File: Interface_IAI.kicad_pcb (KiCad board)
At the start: 2 copper layers, 54 x 63 mm, 20 parts, among them J1 ADWIN_DIO32, J2 ALIM_5V, J3 SCON_PULSE, J4 SCON_FEEDBACK, J5 ADWIN_CO4T, U1 AM26LS31CN, U2 AM26LS32ACN

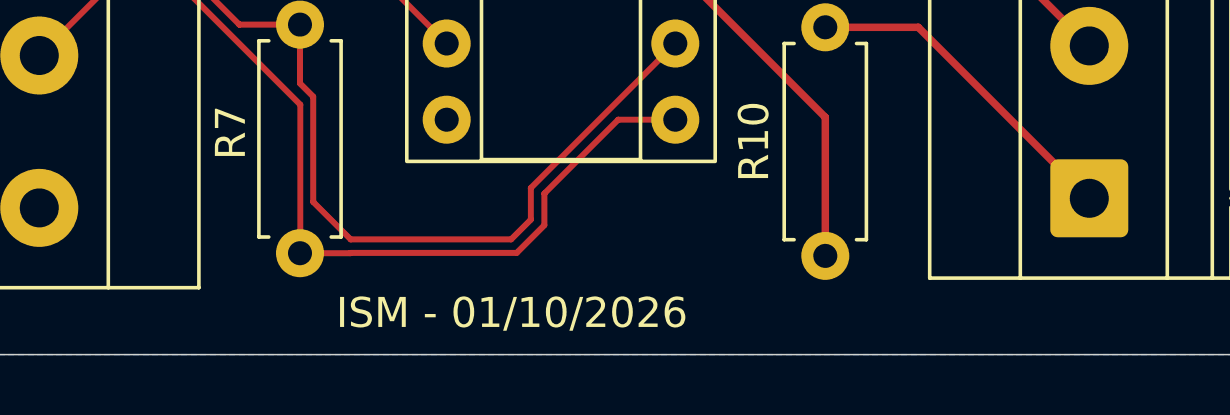
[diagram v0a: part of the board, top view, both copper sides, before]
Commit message: Update PCB silkscreen
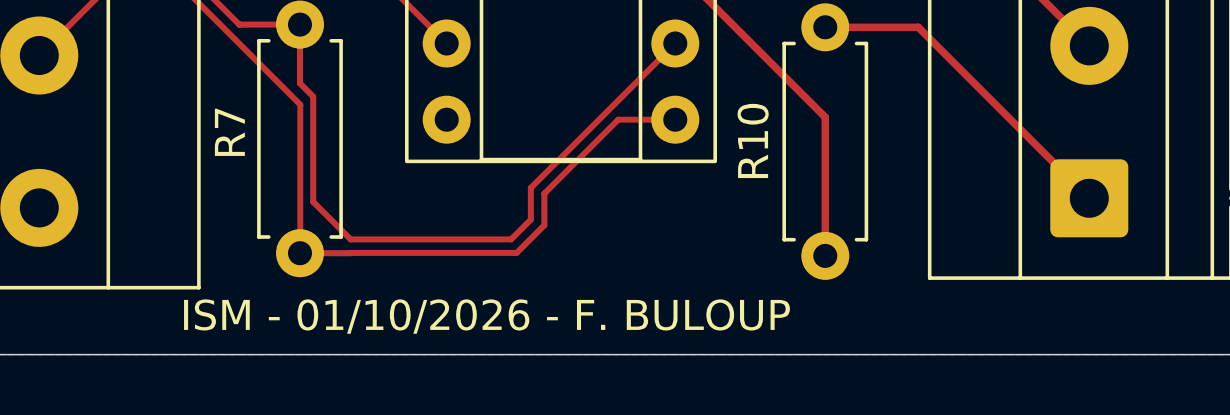
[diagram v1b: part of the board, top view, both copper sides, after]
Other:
- board text added: "ISM - 01/10/2026 - F. BULOUP"
- board text removed: "ISM - 01/10/2026"
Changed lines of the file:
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@@
 		(layer "Edge.Cuts")
 	)
-	(gr_text "ISM - 01/10/2026"
-		(at 69.6 112.2 0)
+	(gr_text "ISM - 01/10/2026 - F. BULOUP"
+		(at 64.4 112.3 0)
 		(layer "F.SilkS")
 		(effects

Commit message: Update board
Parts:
- removed C2: 10uF, Capacitor_THT:C_Disc_D5.0mm_W2.5mm_P5.00mm
- added C4: 10uF, Capacitor_THT:C_Disc_D5.0mm_W2.5mm_P5.00mm, F.Cu at (71.1, 82.6)
- added C5: 10uF 50V, Capacitor_THT:C_Disc_D5.0mm_W2.5mm_P5.00mm, F.Cu at (87.4, 87.3)
- added C6: 100nF, Capacitor_THT:C_Disc_D5.0mm_W2.5mm_P5.00mm, F.Cu at (82.6, 117.4)
- added D1: 1N5819, Diode_THT:D_DO-41_SOD81_P10.16mm_Horizontal, F.Cu at (94.3, 92.7)
- added H1: MountingHole, MountingHole:MountingHole_2.2mm_M2, F.Cu at (109.0, 53.0)
- added H2: MountingHole, MountingHole:MountingHole_2.2mm_M2, F.Cu at (109.0, 167.0)
- added H3: MountingHole, MountingHole:MountingHole_2.2mm_M2, F.Cu at (53.0, 53.0)
- added H4: MountingHole, MountingHole:MountingHole_2.2mm_M2, F.Cu at (53.1, 167.0)
- added J6: ADWin CO4-T, TerminalBlock_Phoenix:TerminalBlock_Phoenix_MKDS-1,5-4-5.08_1x04_P5.08mm_Horizontal, F.Cu at (100.6, 70.9)
- added R11: 10k, Resistor_THT:R_Axial_DIN0207_L6.3mm_D2.5mm_P7.62mm_Horizontal, F.Cu at (82.7, 137.9)
- added R12: 10k, Resistor_THT:R_Axial_DIN0207_L6.3mm_D2.5mm_P7.62mm_Horizontal, F.Cu at (83.0, 133.7)
- added R13: 10k, Resistor_THT:R_Axial_DIN0207_L6.3mm_D2.5mm_P7.62mm_Horizontal, F.Cu at (82.9, 128.9)
- added R14: 10k, Resistor_THT:R_Axial_DIN0207_L6.3mm_D2.5mm_P7.62mm_Horizontal, F.Cu at (82.9, 124.4)
- added R15: 10k, Resistor_THT:R_Axial_DIN0207_L6.3mm_D2.5mm_P7.62mm_Horizontal, F.Cu at (71.3, 145.6)
- added R16: 10k, Resistor_THT:R_Axial_DIN0207_L6.3mm_D2.5mm_P7.62mm_Horizontal, F.Cu at (71.5, 150.4)
- added R17: 10k, Resistor_THT:R_Axial_DIN0207_L6.3mm_D2.5mm_P7.62mm_Horizontal, F.Cu at (71.6, 155.4)
- added R18: 10k, Resistor_THT:R_Axial_DIN0207_L6.3mm_D2.5mm_P7.62mm_Horizontal, F.Cu at (71.5, 160.3)
- added R19: 2.2k, Resistor_THT:R_Axial_DIN0207_L6.3mm_D2.5mm_P7.62mm_Horizontal, F.Cu at (81.9, 145.6)
- added R20: 2.2k, Resistor_THT:R_Axial_DIN0207_L6.3mm_D2.5mm_P7.62mm_Horizontal, F.Cu at (82.2, 150.3)
- added R21: 2.2k, Resistor_THT:R_Axial_DIN0207_L6.3mm_D2.5mm_P7.62mm_Horizontal, F.Cu at (82.1, 155.4)
- added R22: 2.2k, Resistor_THT:R_Axial_DIN0207_L6.3mm_D2.5mm_P7.62mm_Horizontal, F.Cu at (82.1, 160.4)
- added U3: TBD62783APG, Package_DIP:DIP-18_W7.62mm_Socket, F.Cu at (79.5, 137.8)
- added U4: TSR1-2450E, Converter_DCDC:Converter_DCDC_TRACO_TSR-1_THT, F.Cu at (81.7, 83.1)
- J1: value ADWIN_DIO32 -> +24V; footprint TerminalBlock_Phoenix:TerminalBlock_Phoenix_MKDS-1,5-3-5.08_1x03_P5.08mm_Horizontal -> TerminalBlock_Phoenix:TerminalBlock_Phoenix_MKDS-1,5-2-5.08_1x02_P5.08mm_Horizontal
- J2: value ALIM_5V -> ADWIN_DIO32; footprint TerminalBlock_Phoenix:TerminalBlock_Phoenix_MKDS-1,5-2-5.08_1x02_P5.08mm_Horizontal -> TerminalBlock_Phoenix:TerminalBlock_Phoenix_MKDS-1,5-11-5.08_1x11_P5.08mm_Horizontal
- J3: value SCON_PULSE -> SCON_FEEDBACK; footprint TerminalBlock_Phoenix:TerminalBlock_Phoenix_MKDS-1,5-4-5.08_1x04_P5.08mm_Horizontal -> TerminalBlock_Phoenix:TerminalBlock_Phoenix_MKDS-1,5-7-5.08_1x07_P5.08mm_Horizontal
- J4: value SCON_FEEDBACK -> SCON_PULSE; footprint TerminalBlock_Phoenix:TerminalBlock_Phoenix_MKDS-1,5-7-5.08_1x07_P5.08mm_Horizontal -> TerminalBlock_Phoenix:TerminalBlock_Phoenix_MKDS-1,5-4-5.08_1x04_P5.08mm_Horizontal
- J5: value ADWIN_CO4T -> SCON_PIO; footprint TerminalBlock_Phoenix:TerminalBlock_Phoenix_MKDS-1,5-4-5.08_1x04_P5.08mm_Horizontal -> TerminalBlock_Phoenix:TerminalBlock_Phoenix_MKDS-1,5-10-5.08_1x10_P5.08mm_Horizontal
- U1: value AM26LS31CN -> AM26LS31
- U2: value AM26LS32ACN -> AM26LS32
- moved J2 84.8 mm to (100.8, 162.9)
- moved R4 52.9 mm to (82.0, 111.5), turned to 90 degrees
- moved R2 49.9 mm to (85.3, 103.9), turned to -90 degrees
- moved R10 41.1 mm to (84.9, 68.6), turned to 0 degrees
- moved R9 35.4 mm to (84.9, 63.7), turned to 0 degrees
- moved J5 34.6 mm to (61.4, 117.2), turned to -90 degrees
- moved U2 33.1 mm to (73.6, 54.3)
- moved C3 30.2 mm to (84.2, 54.1), turned to 0 degrees
- moved R1 29.3 mm to (89.1, 97.0)
- moved R7 29.1 mm to (81.0, 75.7), turned to 180 degrees
- moved R3 28.7 mm to (81.5, 100.6)
- moved R8 28.0 mm to (84.9, 60.3), turned to 0 degrees
- moved R6 27.1 mm to (69.7, 64.1)
- moved R5 26.9 mm to (69.7, 61.3)
- moved U1 22.0 mm to (70.0, 93.1), turned to 0 degrees
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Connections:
- J1 pad 1: /DIO_PULSE -> +24V
- J2 pad 1: +5V -> GND
- J2 pad 2: GND -> /DIO_ALM
- J3 pad 1: /SIGN_P -> /FB_A_N
- J3 pad 2: /SIGN_N -> /FB_A_P
- J3 pad 3: /PULSE_N -> /FB_B_P
- J3 pad 4: /PULSE_P -> /FB_B_N
- J4 pad 1: /FB_A_N -> /PULSE_P
- J4 pad 2: /FB_A_P -> /PULSE_N
- J4 pad 3: /FB_B_P -> /SIGN_N
- J4 pad 4: /FB_B_N -> /SIGN_P
- J5 pad 1: /CNT_Z -> +24V
- J5 pad 2: /CNT_B -> GND
- J5 pad 3: /CNT_A -> /SCON_CSTP
- J5 pad 4: GND -> /SCON_HOME
- U1 pad 4: +5V -> GND
- U2 pad 4: +5V -> GND
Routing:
- net +24V: track 0.00 -> 80.4 mm
- net /PULSE_P: track 44.9 -> 12.0 mm
- net /PULSE_N: track 39.5 -> 9.23 mm
- net /DIO_CSTP: track 0.00 -> 25.9 mm
- net /DIO_HOME: track 0.00 -> 23.8 mm
- net /DIO_RES: track 0.00 -> 23.7 mm
- net /DIO_SV: track 0.00 -> 23.1 mm
- net /DIO_INP: track 0.00 -> 22.8 mm
- net /DIO_ALM: track 0.00 -> 22.8 mm
- net /DIO_HEND: track 0.00 -> 22.7 mm
- net /DIO_SON: track 0.00 -> 22.7 mm
- net /SIGN_N: track 29.8 -> 9.23 mm
- net /DIO_PULSE: track 0.00 -> 20.0 mm
- net /PULSE_TTL: track 0.00 -> 16.7 mm
- net /VIN_REG: track 0.00 -> 16.5 mm
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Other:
- board size 54 x 63 mm -> 62 x 120 mm
- board text added: "+24V"
- board text added: "A"
- board text added: "ADWin - DIO32"
- board text added: "ADWin CO4-T"
- board text added: "ALIM+24V"
- board text added: "ALM"
- board text added: "B"
- board text added: "CSTP"
- board text added: "HEND"
- board text added: "HOME"
- board text added: "INP"
- board text added: "ISM - 04/10/2026 F.BULOUP"
- board text added: "PULSE_N"
- board text added: "PULSE_P"
- board text added: "RES"
- board text added: "SCON FEEDBACK"
- board text added: "SCON PIO"
- board text added: "SCON PULSE"
- board text added: "SIGN_N"
- board text added: "SIGN_P"
- board text added: "SON"
- board text added: "SV"
- board text added: "Z"
- board text removed: "+"
- board text removed: "+5V"
- board text removed: "ADWIN_CO4_T"
- board text removed: "ADWIN_DIO32"
- board text removed: "ALIM_5V"
- board text removed: "CNT_A"
- board text removed: "CNT_B"
- board text removed: "CNT_Z"
- board text removed: "ISM - 01/10/2026 - F. BULOUP"
- board text removed: "P_N"
- board text removed: "P_P"
- board text removed: "SCON_FEEDBACK"
- board text removed: "SCON_PULSE_SIGN"
- board text removed: "S_N"
- board text removed: "S_P"

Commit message: Modify BOM
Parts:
- C5: footprint Capacitor_THT:C_Disc_D5.0mm_W2.5mm_P5.00mm -> Capacitor_THT:C_Radial_D5.0mm_H11.0mm_P2.00mm
- moved C5 3.20 mm to (90.1, 85.5)
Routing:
- net /VIN_REG: track 16.5 -> 18.2 mm
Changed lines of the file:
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@@
 		(tags "THT Terminal Block Phoenix MKDS-1,5-11-5.08 pitch 5.08mm size 55.9x9.8mm drill 1.3mm pad 2.6mm")
 		(property "Reference" "J2"
-			(at 54.98 -0.18 0)
+			(at 54.843553 1.401374 0)
 			(layer "F.SilkS")
 			(effects
@@
 		)
 	)
-	(footprint "Capacitor_THT:C_Disc_D5.0mm_W2.5mm_P5.00mm"
+	(footprint "Capacitor_THT:C_Radial_D5.0mm_H11.0mm_P2.00mm"
 		(layer "F.Cu")
-		(at 87.398626 87.303553 90)
-		(descr "C, Disc series, Radial, pin pitch=5.00mm, diameter*width=5*2.5mm^2, Capacitor, http://cdn-reichelt.de/documents/datenblatt/B300/DS_KERKO_TC.pdf")
-		(tags "C Disc series Radial pin pitch 5.00mm diameter 5mm width 2.5mm Capacitor")
+		(at 90.07 85.54 90)
+		(descr "C, Radial series, Radial, pin pitch=2.00mm, diameter=5mm, height=11mm, Non-Polar Electrolytic Capacitor")
+		(tags "C Radial series Radial pin pitch 2.00mm diameter 5mm height 11mm Non-Polar Electrolytic Capacitor")
 		(property "Reference" "C5"
-			(at 6.9 -0.2 0)
+			(at 1 -3.75 90)
 			(layer "F.SilkS")
 			(effects
@@
 		)
 		(property "Value" "10uF 50V"
-			(at 2.5 2.5 90)
+			(at 1 3.75 90)
 			(layer "F.Fab")
 			(effects
@@
 		(attr through_hole)
 		(duplicate_pad_numbers_are_jumpers no)
-		(fp_line
-			(start 5.12 -1.37)
-			(end 5.12 -1.033)
-			(stroke
-				(width 0.12)
-				(type solid)
-			)
-			(layer "F.SilkS")
-		)
-		(fp_line
-			(start -0.12 -1.37)
-			(end 5.12 -1.37)
-			(stroke
-				(width 0.12)
-				(type solid)
-			)
-			(layer "F.SilkS")
-		)
-		(fp_line
-			(start -0.12 -1.033)
-			(end -0.12 -1.37)
-			(stroke
-				(width 0.12)
-				(type solid)
-			)
-			(layer "F.SilkS")
-		)
-		(fp_line
-			(start 5.12 1.033)
-			(end 5.12 1.37)
-			(stroke
-				(width 0.12)
-				(type solid)
-			)
-			(layer "F.SilkS")
-		)
-		(fp_line
-			(start 5.12 1.37)
-			(end -0.12 1.37)
-			(stroke
-				(width 0.12)
-				(type solid)
-			)
-			(layer "F.SilkS")
-		)
-		(fp_line
-			(start -0.12 1.37)
-			(end -0.12 1.033)
+		(fp_circle
+			(center 1 0)
+			(end 3.62 0)
 			(stroke
 				(width 0.12)
 				(type solid)
 			)
+			(fill no)
 			(layer "F.SilkS")
 		)
-		(fp_rect
-			(start -1.05 -1.5)
-			(end 6.05 1.5)
+		(fp_circle
+			(center 1 0)
+			(end 3.75 0)
 			(stroke
 				(width 0.05)
@@
 			(layer "F.CrtYd")
 		)
-		(fp_rect
-			(start 0 -1.25)
-			(end 5 1.25)
+		(fp_circle
+			(center 1 0)
+			(end 3.5 0)
 			(stroke
 				(width 0.1)
@@
 		)
 		(fp_text user "${REFERENCE}"
-			(at 2.5 0 90)
+			(at 1 0 90)
 			(layer "F.Fab")
 			(effects
@@
 		)
 		(pad "2" thru_hole circle
-			(at 5 0 90)
+			(at 2 0 90)
 			(size 1.6 1.6)
 			(drill 0.8)
@@
 		)
 		(embedded_fonts no)
-		(model "${KICAD10_3DMODEL_DIR}/Capacitor_THT.3dshapes/C_Disc_D5.0mm_W2.5mm_P5.00mm.step"
+		(model "${KICAD10_3DMODEL_DIR}/Capacitor_THT.3dshapes/C_Radial_D5.0mm_H11.0mm_P2.00mm.step"
 			(offset
 				(xyz 0 0 0)
@@
 	)
 	(segment
-		(start 87.398626 87.303553)
-		(end 88.859109 87.303553)
+		(start 90.07 85.54)
+		(end 84.150073 85.54)
 		(width 1)
 		(layer "F.Cu")
@@
 	)
 	(segment
-		(start 87.398626 87.303553)
-		(end 85.913626 87.303553)
+		(start 94.26 92.704444)
+		(end 94.26 89.73)
 		(width 1)
 		(layer "F.Cu")
@@
 	)
 	(segment
-		(start 85.913626 87.303553)
+		(start 84.150073 85.54)
 		(end 81.731126 83.121053)
 		(width 1)
@@
 	)
 	(segment
-		(start 88.859109 87.303553)
-		(end 94.26 92.704444)
+		(start 94.26 89.73)
+		(end 90.07 85.54)
 		(width 1)
 		(layer "F.Cu")

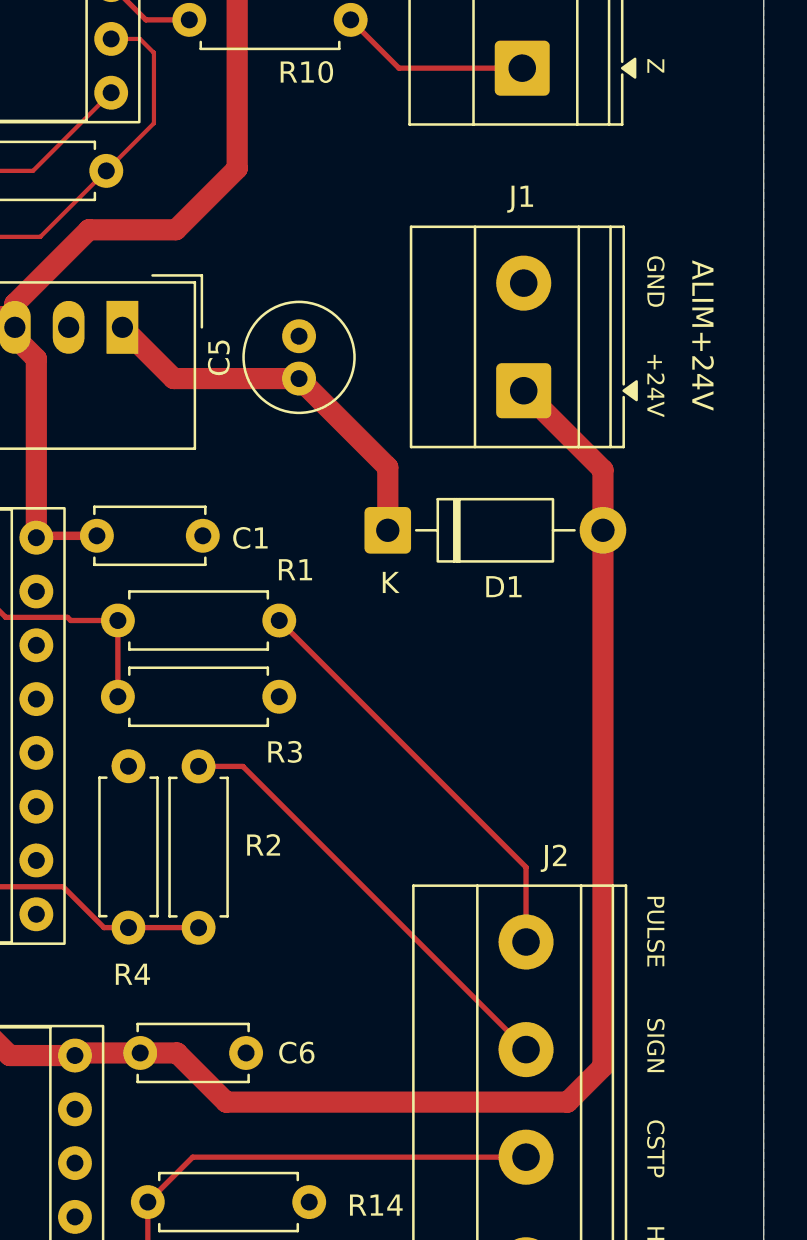
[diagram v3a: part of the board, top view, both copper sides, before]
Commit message: Add DEL Alim.
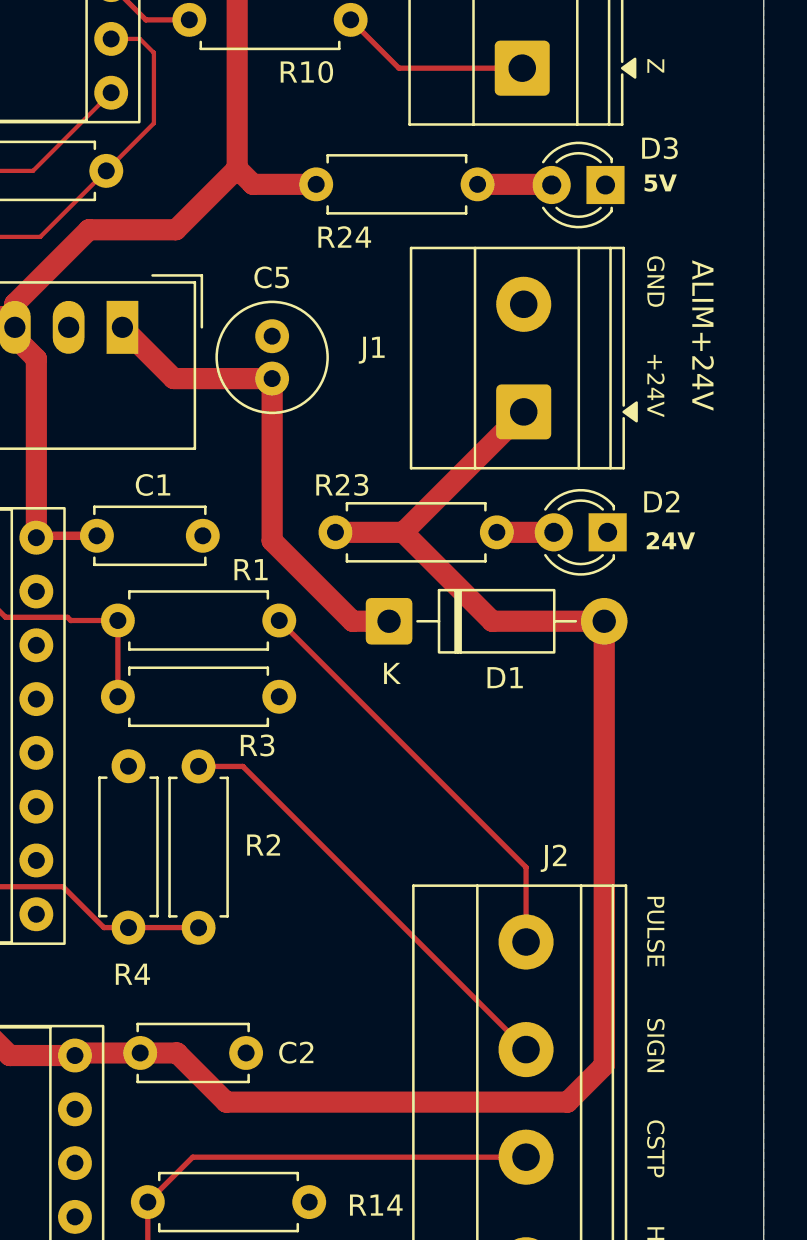
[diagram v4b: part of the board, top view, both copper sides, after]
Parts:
- added D2: WP710A10LGD, LED_THT:LED_D3.0mm, F.Cu at (104.6, 92.8)
- added D3: WP710A10LGD, LED_THT:LED_D3.0mm, F.Cu at (104.5, 76.4)
- added R23: 10k, Resistor_THT:R_Axial_DIN0207_L6.3mm_D2.5mm_P7.62mm_Horizontal, F.Cu at (91.8, 92.8)
- added R24: 2.2k, Resistor_THT:R_Axial_DIN0207_L6.3mm_D2.5mm_P7.62mm_Horizontal, F.Cu at (90.9, 76.4)
- moved D1 4.30 mm to (94.3, 97.0)
- moved C5 1.27 mm to (88.8, 85.5)
- moved J1 1.00 mm to (100.7, 87.1)
- renumbered C6 to C2
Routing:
- net +24V: track 80.4 -> 90.5 mm
- net /VIN_REG: track 18.2 -> 22.8 mm
- net +5V: track 65.5 -> 69.6 mm
- net Net-(D3-A): track 0.00 -> 3.51 mm
- net Net-(D2-A): track 0.00 -> 2.69 mm
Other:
- board text added: "24V"
- board text added: "5V"

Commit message: Update Doc. and Gerber files
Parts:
- removed H1, H2, H3, H4: MountingHole, MountingHole:MountingHole_2.2mm_M2
- moved C2 18.4 mm to (101.0, 117.4)
- moved C4 18.4 mm to (89.5, 82.6)
- moved C5 18.4 mm to (107.2, 85.6)
- moved D1 18.4 mm to (112.7, 97.0)
- moved D2 18.4 mm to (123.0, 92.8)
- moved J1 18.4 mm to (119.1, 87.1)
- moved J2 18.4 mm to (119.2, 163.0)
- moved J3 18.4 mm to (79.7, 55.8)
- moved J6 18.4 mm to (119.0, 70.9)
- moved R11 18.4 mm to (101.1, 137.9)
- moved R12 18.4 mm to (101.4, 133.7)
- moved R15 18.4 mm to (89.7, 145.6)
- moved R16 18.4 mm to (89.9, 150.4)
- moved R17 18.4 mm to (90.0, 155.4)
- moved R20 18.4 mm to (100.6, 150.3)
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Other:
- board size 62 x 120 mm -> 98.8 x 120 mm

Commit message: Update gerber files
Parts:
- moved C4 0.59 mm to (89.4, 83.2)
- moved C5 0.59 mm to (107.1, 86.1)
- moved J6 0.59 mm to (118.9, 71.5)
- moved R24 0.59 mm to (109.2, 77.0)
- moved R4 0.59 mm to (100.3, 112.1)
- moved U1 0.59 mm to (88.3, 93.7)
- moved C1 0.59 mm to (98.8, 93.6)
- moved C2 0.59 mm to (100.9, 118.0)
- moved C3 0.59 mm to (102.5, 54.7)
- moved D3 0.59 mm to (122.8, 77.0)
- moved R1 0.59 mm to (107.4, 97.6)
- moved R10 0.59 mm to (103.2, 69.2)
- moved R2 0.59 mm to (103.6, 104.5)
- moved R9 0.59 mm to (103.2, 64.3)
- moved U4 0.59 mm to (100.0, 83.7)
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
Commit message: Update Doc.
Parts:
- added F1: Polyfuse, MF-R050:MFR050, F.Cu at (106.4, 97.7)
- added H1: MountingHole, MountingHole:MountingHole_3.2mm_M3, F.Cu at (57.6, 57.5)
- added H2: MountingHole, MountingHole:MountingHole_3.2mm_M3, F.Cu at (57.6, 120.5)
- added H3: MountingHole, MountingHole:MountingHole_3.2mm_M3, F.Cu at (57.6, 183.4)
- added H4: MountingHole, MountingHole:MountingHole_3.2mm_M3, F.Cu at (121.7, 57.5)
- added H5: MountingHole, MountingHole:MountingHole_3.2mm_M3, F.Cu at (121.7, 120.5)
- added H6: MountingHole, MountingHole:MountingHole_3.2mm_M3, F.Cu at (121.7, 183.4)
- added R25: 10k, Resistor_THT:R_Axial_DIN0207_L6.3mm_D2.5mm_P7.62mm_Horizontal, F.Cu at (89.8, 136.5)
- added R26: 10k, Resistor_THT:R_Axial_DIN0207_L6.3mm_D2.5mm_P7.62mm_Horizontal, F.Cu at (89.8, 132.4)
- added R27: 2.2k, Resistor_THT:R_Axial_DIN0207_L6.3mm_D2.5mm_P7.62mm_Horizontal, F.Cu at (89.7, 163.2)
- added R28: 10k, Resistor_THT:R_Axial_DIN0207_L6.3mm_D2.5mm_P7.62mm_Horizontal, F.Cu at (78.9, 163.2)
- added R29: 2.2k, Resistor_THT:R_Axial_DIN0207_L6.3mm_D2.5mm_P7.62mm_Horizontal, F.Cu at (89.7, 158.4)
- added R30: 10k, Resistor_THT:R_Axial_DIN0207_L6.3mm_D2.5mm_P7.62mm_Horizontal, F.Cu at (78.9, 158.4)
- C5: footprint Capacitor_THT:C_Radial_D5.0mm_H11.0mm_P2.00mm -> Capacitor_THT:CP_Radial_D5.0mm_P2.00mm
- J2: value ADWIN_DIO32 -> Screw_Terminal_01x15; footprint TerminalBlock_Phoenix:TerminalBlock_Phoenix_MKDS-1,5-11-5.08_1x11_P5.08mm_Horizontal -> TerminalBlock_Phoenix:TerminalBlock_Phoenix_MKDS-1,5-15-5.08_1x15_P5.08mm_Horizontal
- J5: value SCON_PIO -> Screw_Terminal_01x14; footprint TerminalBlock_Phoenix:TerminalBlock_Phoenix_MKDS-1,5-10-5.08_1x10_P5.08mm_Horizontal -> TerminalBlock_Phoenix:TerminalBlock_Phoenix_MKDS-1,5-14-5.08_1x14_P5.08mm_Horizontal
- moved R20 24.5 mm to (89.7, 173.0)
- moved R17 24.5 mm to (79.2, 178.1)
- moved R21 24.5 mm to (89.7, 178.1)
- moved R22 24.5 mm to (89.7, 183.1)
- moved R15 24.5 mm to (78.9, 168.3)
- moved R16 24.5 mm to (79.1, 173.1)
- moved R18 24.5 mm to (79.2, 183.0)
- moved R19 24.4 mm to (89.7, 168.3)
- moved J2 22.6 mm to (109.1, 183.9)
- moved R12 19.5 mm to (89.7, 150.0)
- moved R14 19.5 mm to (89.7, 140.7)
- moved R13 19.5 mm to (89.7, 145.2)
- moved R11 19.3 mm to (89.7, 154.2)
- moved C2 15.9 mm to (88.8, 128.4)
- moved U3 15.8 mm to (85.8, 148.7)
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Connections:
- net /PULSE_N renamed /PP_N
- net /PULSE_P renamed /PP_P
- net /PULSE_TTL renamed /PP_TTL
- net /SIGN_N renamed /NP_N
- net /SIGN_P renamed /NP_P
- net /SIGN_TTL renamed /NP_TTL
- C5 pad 1: /VIN_REG -> +24V
- D1 pad 1: /VIN_REG -> +24V
- D1 pad 2: +24V -> Net-(D1-A)
- J1 pad 1: +24V -> Net-(J1-Pin_1)
- J2 pad 10: /DIO_SIGN -> /DIO_HOME
- J2 pad 11: /DIO_PULSE -> /DIO_CSTP
- J2 pad 6: /DIO_SON -> /DIO_IN0
- J2 pad 7: /DIO_RES -> /DIO_IN1
- J2 pad 8: /DIO_HOME -> /DIO_SON
- J2 pad 9: /DIO_CSTP -> /DIO_RES
- J5 pad 10: /SCON_ALM -> /SCON_OUT0
- J5 pad 3: /SCON_CSTP -> /SCON_IN1
- J5 pad 4: /SCON_HOME -> /SCON_IN0
- J5 pad 5: /SCON_RES -> /SCON_CSTP
- J5 pad 6: /SCON_SON -> /SCON_HOME
- J5 pad 7: /SCON_SV -> /SCON_RES
- J5 pad 8: /SCON_INP -> /SCON_SON
- J5 pad 9: /SCON_HEND -> /SCON_OUT1
- R1 pad 1: /DIO_PULSE -> /DIO_PP
- R2 pad 1: /DIO_SIGN -> /DIO_NP
- U3 pad 13: unconnected-(U3-O6-Pad13) -> /SCON_IN1
- U3 pad 14: unconnected-(U3-O5-Pad14) -> /SCON_IN0
- U3 pad 5: GND -> /DIO_OUT0
- U3 pad 6: GND -> /DIO_OUT1
- U4 pad 1: /VIN_REG -> +24V
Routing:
- net /DIO_OUT1: track 0.00 -> 28.4 mm
- net /DIO_OUT0: track 0.00 -> 27.6 mm
- net /DIO_IN1: track 0.00 -> 24.6 mm
- net /DIO_IN0: track 0.00 -> 24.5 mm
- net /DIO_PP: track 0.00 -> 23.9 mm
- net /DIO_NP: track 0.00 -> 23.7 mm
- net /VIN_REG: track 22.8 -> 0.00 mm
- net /DIO_SIGN: track 21.0 -> 0.00 mm
- net /DIO_PULSE: track 20.0 -> 0.00 mm
- net Net-(J1-Pin_1): track 0.00 -> 14.9 mm
- net +24V: track 90.5 -> 101.9 mm
- net /SCON_IN1: track 0.00 -> 11.4 mm
- net /SCON_IN0: track 0.00 -> 11.0 mm
- net /SCON_OUT0: track 0.00 -> 9.58 mm
- net /SCON_OUT1: track 0.00 -> 9.35 mm
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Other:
- board size 98.8 x 120 mm -> 79.3 x 141 mm
- board text added: "IN0"
- board text added: "IN1"
- board text added: "NP"
- board text added: "NP_N"
- board text added: "NP_P"
- board text added: "OUT0"
- board text added: "OUT1"
- board text added: "PP"
- board text added: "PP_N"
- board text added: "PP_P"
- board text removed: "PULSE"
- board text removed: "PULSE_N"
- board text removed: "PULSE_P"
- board text removed: "SIGN"
- board text removed: "SIGN_N"
- board text removed: "SIGN_P"
